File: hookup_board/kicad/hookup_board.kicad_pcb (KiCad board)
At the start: 2 copper layers, 90 x 88.4 mm, 876 parts, among them J1 pcie_98

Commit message: Add more progress on the hookup board's layout.
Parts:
- removed REF** (x873): pad, hookup_board:pad
- J1: footprint common:PCIE_98_CARD -> hookup_board:PCIE_98_MINI_CARD
- locked (x2): footprint hookup_board:PinHeader_2x25_P2.00mm_Vertical_SMD -> hookup_board:PinHeader_2x25_P2.54mm_Vertical
- moved locked 30.6 mm to (-17.0, -17.7)
- moved locked 30.5 mm to (-17.0, -11.2)
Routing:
- net /B8: track 11.8 -> 0.00 mm
- net /B26: track 11.8 -> 0.00 mm
- net /B6: track 11.8 -> 0.00 mm
- net /B40: track 11.8 -> 0.00 mm
- net /B42: track 11.8 -> 0.00 mm
- net /B38: track 11.8 -> 0.00 mm
- net /B36: track 11.8 -> 0.00 mm
- net /B34: track 11.8 -> 0.00 mm
- net /B32: track 11.8 -> 0.00 mm
- net /B30: track 11.8 -> 0.00 mm
- net /B28: track 11.8 -> 0.00 mm
- net /B24: track 11.8 -> 0.00 mm
- net /B22: track 11.8 -> 0.00 mm
- net /B20: track 11.8 -> 0.00 mm
- net /B18: track 11.8 -> 0.00 mm
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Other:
- board size 90 x 88.4 mm -> 68.6 x 24 mm
- board text added: "Hookup Board Ver 0.2"
- board text added: "XYZ"
- board text removed: "10"
- board text removed: "19"
- board text removed: "2"
- board text removed: "20"
- board text removed: "29"
- board text removed: "30"
- board text removed: "39"
- board text removed: "40"
- board text removed: "50"
- board text removed: "9"
- board text removed: "A"
- board text removed: "B"
- board text removed: "Proto Board Ver 0.2"

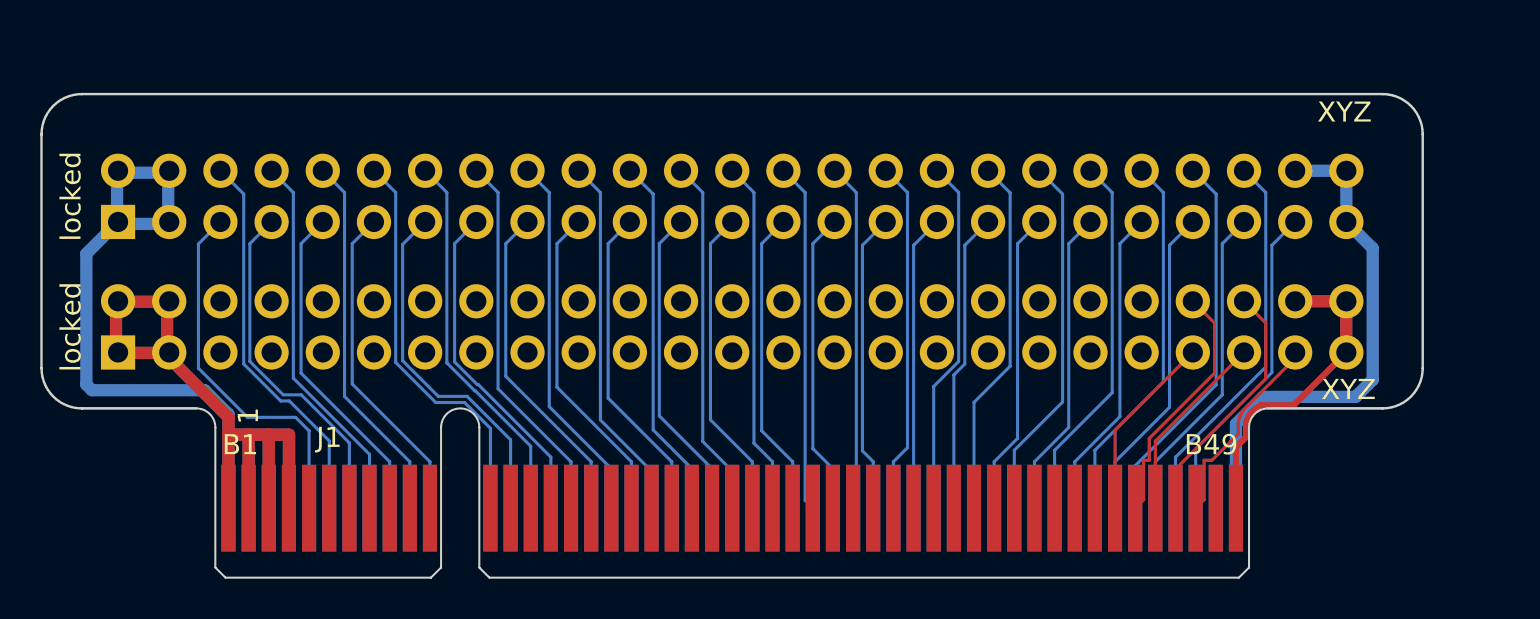
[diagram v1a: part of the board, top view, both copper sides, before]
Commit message: Completed the layout of the hookup board.
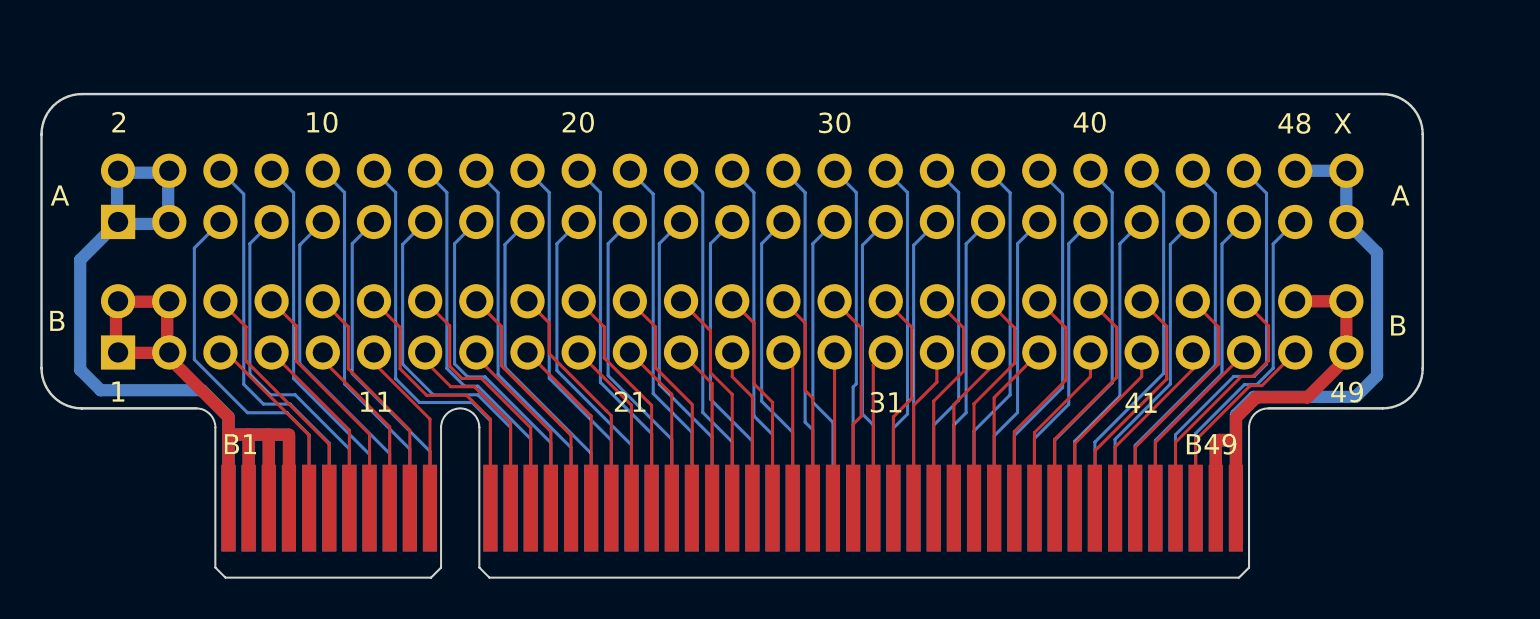
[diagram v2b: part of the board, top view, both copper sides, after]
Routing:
- net /B12: track 0.00 -> 13.8 mm
- net /B14: track 0.00 -> 13.0 mm
- net /B6: track 0.00 -> 12.5 mm
- net /B8: track 0.00 -> 12.3 mm
- net /B42: track 0.00 -> 12.3 mm
- net /B16: track 0.00 -> 12.2 mm
- net /B40: track 0.00 -> 12.1 mm
- net /B10: track 0.00 -> 12.1 mm
- net /B18: track 0.00 -> 12.0 mm
- net /B38: track 0.00 -> 11.9 mm
- net /B20: track 0.00 -> 11.8 mm
- net /B36: track 0.00 -> 11.7 mm
- net /B22: track 0.00 -> 11.5 mm
- net /B34: track 0.00 -> 11.4 mm
- net /B24: track 0.00 -> 11.3 mm
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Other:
- board text added: "10"
- board text added: "11"
- board text added: "2"
- board text added: "20"
- board text added: "21"
- board text added: "30"
- board text added: "31"
- board text added: "40"
- board text added: "41"
- board text added: "48"
- board text added: "49"
- board text added: "A"
- board text added: "B"
- board text added: "V 0.1"
- board text added: "X"
- board text removed: "XYZ"
